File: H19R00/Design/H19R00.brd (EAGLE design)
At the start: 60 x 60.6 mm, 112 parts, among them J1 691213710003, J2 691213710002, J3 20021121-00008T4LFU, J4 20021121-00006C1LF, U1 STM32G0B1CEU6N, U2 STSPIN32F0A, U3 AM26LV32EIRGYRTEXAS_INSTRUMEN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, U4 NCP730BMTADJTBGON_SEMI_NCP730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, X1 8MHZ

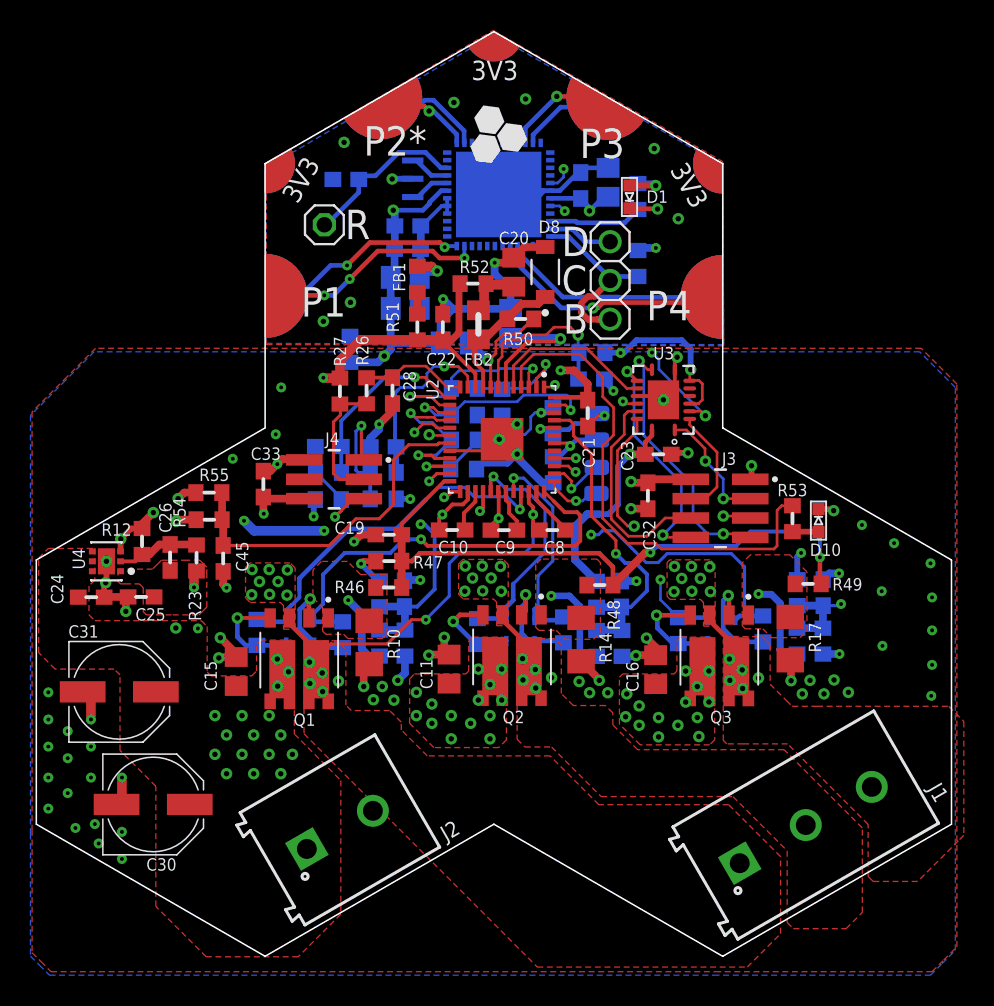
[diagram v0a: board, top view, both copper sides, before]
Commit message: -Add some notes to the schematic -fix the BOM - Add NRST,TX1 and RX1  test points -Fix some issues at the silkscreen layer
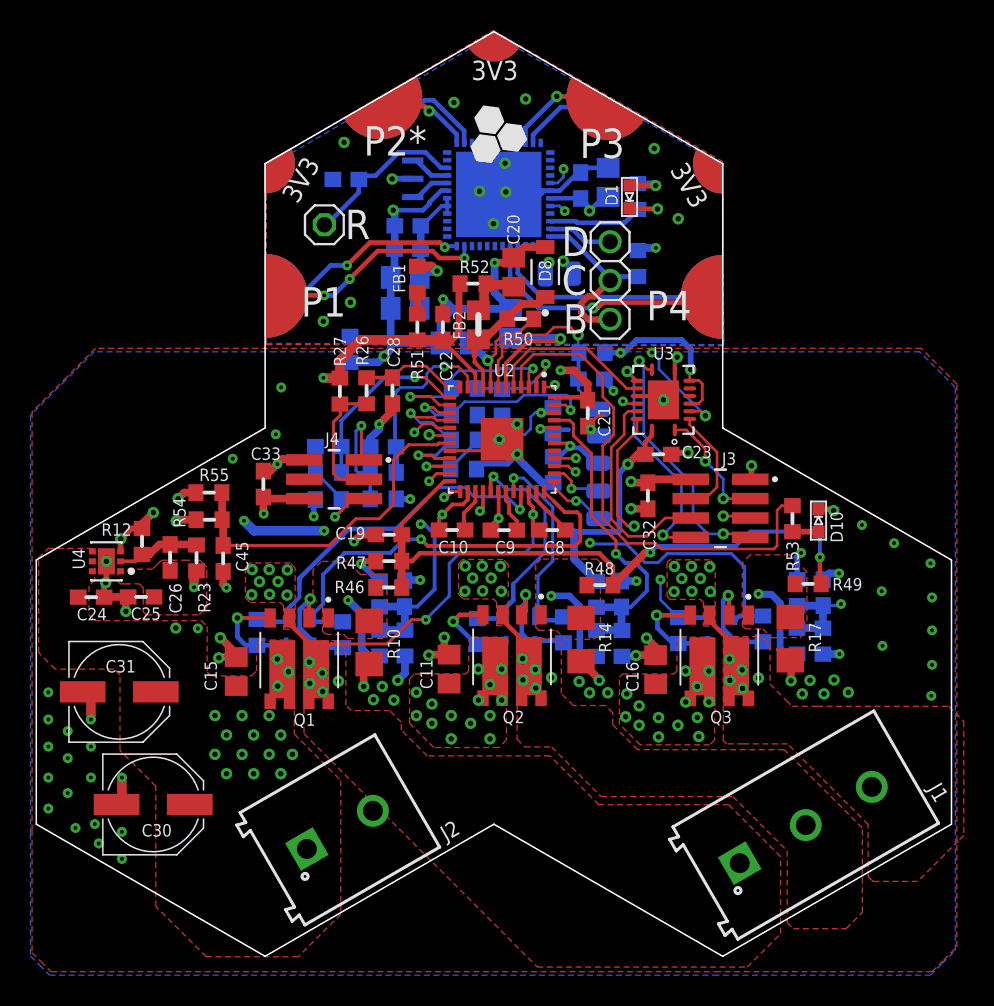
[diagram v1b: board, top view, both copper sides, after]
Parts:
- added NRST, RX1, TX1: PAD4, HEXABITZ_CONNECTION_PARTS:PAD4
- moved SWDIO 1.66 mm to (6.85, 20.0)
- moved SWDCLK 1.55 mm to (6.85, 21.8)
- moved BOOT0 1.53 mm to (6.83, 23.7)
- moved GND 1.48 mm to (6.90, 25.4)
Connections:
- net G0_USART1_RX: now also RX1.P$1
- net G0_USART1_TX: now also TX1.P$1
- net GND: no longer U1.11, U1.12
- net N$14: now also NRST.P$1
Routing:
- net G0_USART1_TX: track 28.9 -> 36.3 mm, vias 2 -> 3
- net G0_USART1_RX: track 25.6 -> 30.0 mm, vias 2 -> 3
- net GND1: track 109.9 -> 107.0 mm
- net N$14: track 11.5 -> 14.0 mm
- net VDD_L: track 120.7 -> 121.8 mm
- net USART5_TX: track 15.6 -> 16.5 mm
- net USART5_RX: track 14.4 -> 15.2 mm
- net GND: vias 10 -> 14
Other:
- board text added: "38V MAX"
- board text removed: "38V"
